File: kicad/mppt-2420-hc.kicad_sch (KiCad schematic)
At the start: 18 parts, among them J1 MKDS 5/ 2-9,5, J2 MKDS 5/ 2-9,5, J3 MKDS 5/ 2-9,5, J4 8P8C, J5 8P8C, J6 JST PH

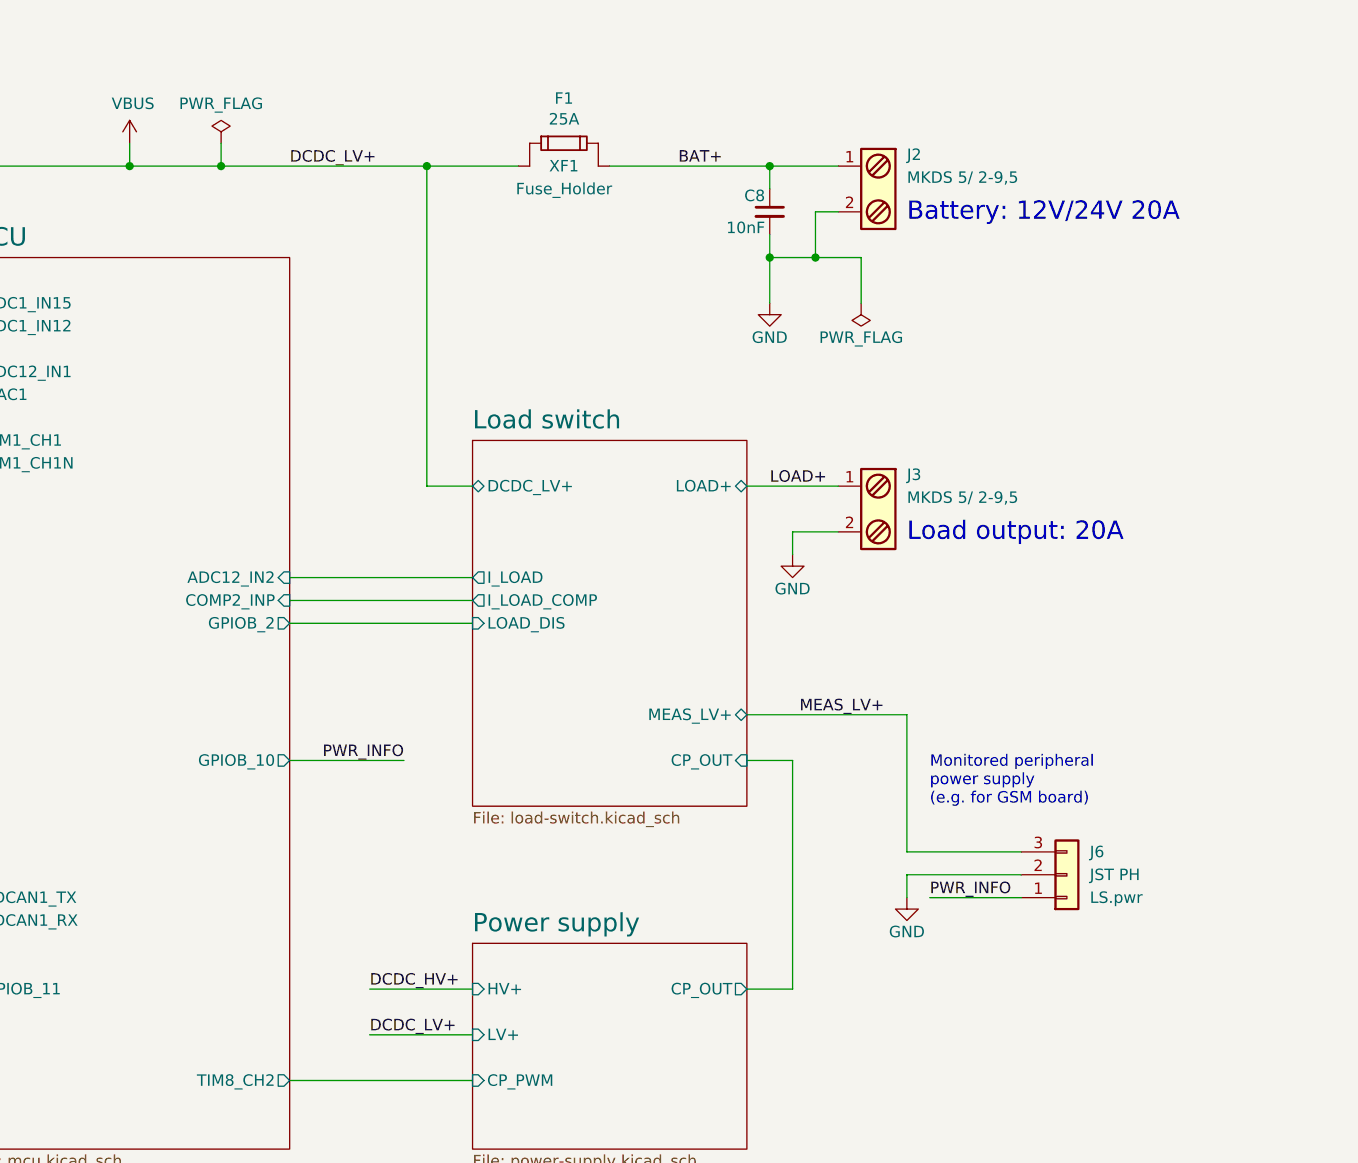
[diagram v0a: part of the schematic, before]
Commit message: removed load terminal & circuit
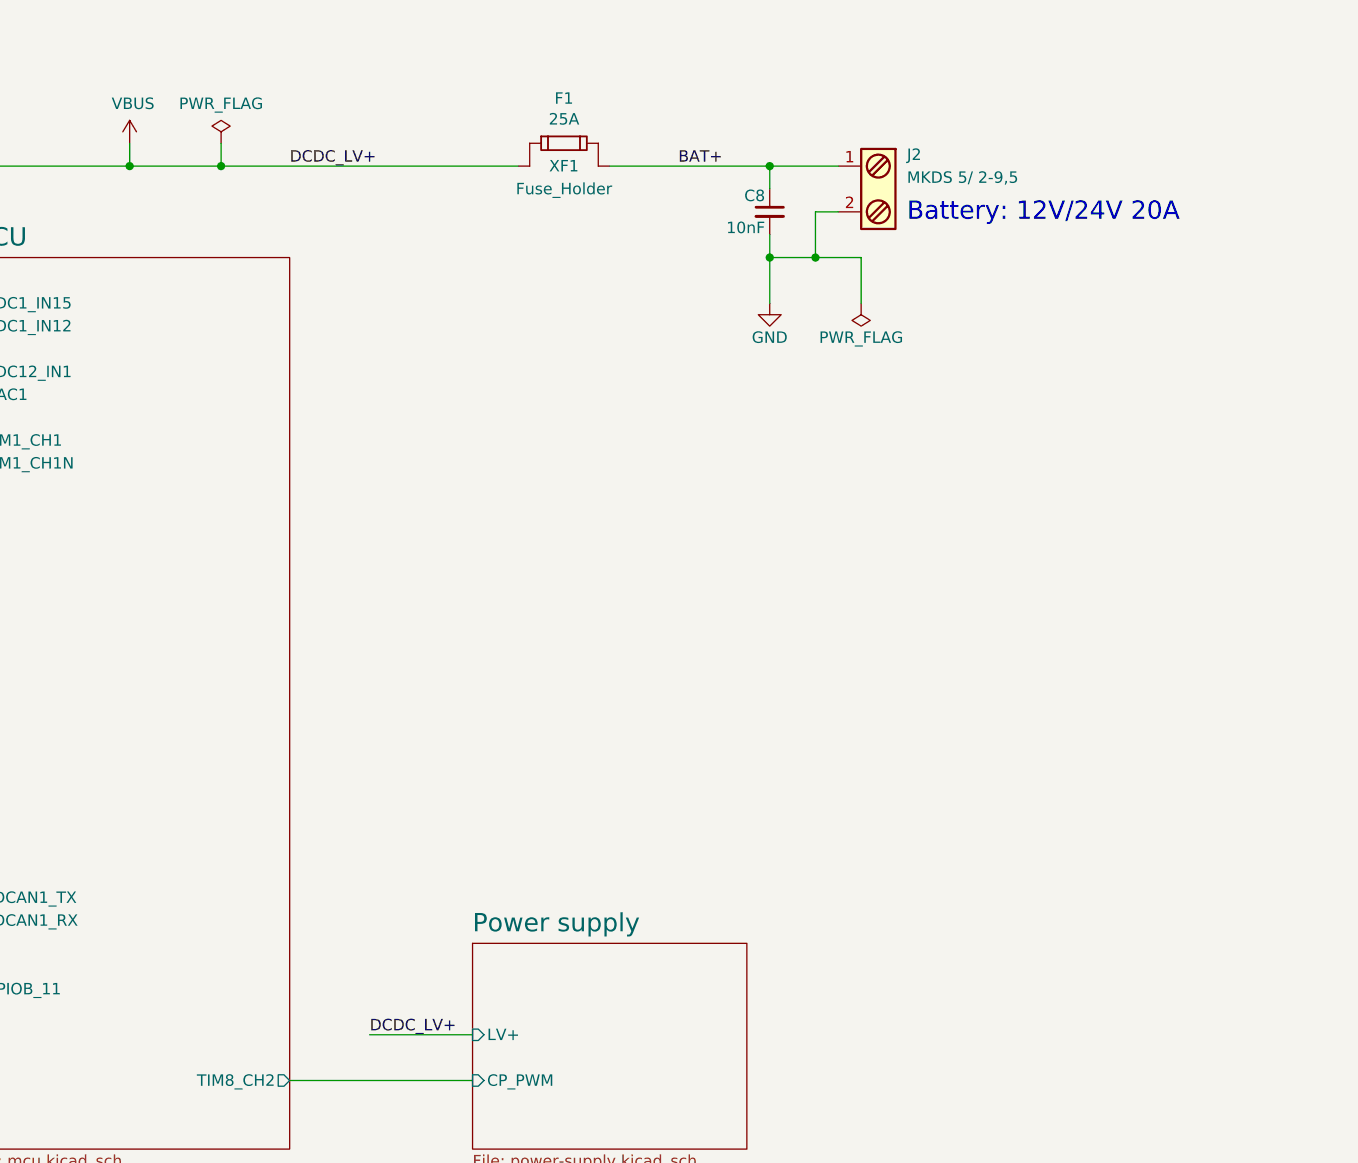
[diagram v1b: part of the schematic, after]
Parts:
- removed J3: MKDS 5/ 2-9,5, LibreSolar:Phoenix_Contact_MKDS_5-2-9,5, symbol Project:Screw_Terminal_1x02
- removed J6: JST PH, Connector_JST:JST_PH_B3B-PH-K_1x03_P2.00mm_Vertical, symbol Connector_Generic:Conn_01x03
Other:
- removed sheet Load switch
- sheet MCU ports: added none; removed ADC12_IN2, COMP2_INP, GPIOB_10, GPIOB_2
- sheet Power supply ports: added none; removed CP_OUT, HV+
- note removed: "Load output: 20A"
- note removed: "Monitored peripheral power supply (e.g. for GSM board)"

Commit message: major changes
removed Load terminal

changed to 6.3x32mm fuse pcb holder

added LibreSolar kicad footprint library locally
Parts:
- XF1: footprint LibreSolar:Keystone-Fuse-3557-2 -> LibreSolar:Eaton_S-400; Manufacturer Keystone -> Eaton; PartNumber 3557-2 -> (none)
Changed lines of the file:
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@@
     (property "Reference" "XF1" (id 0) (at 198.12 48.26 0))
     (property "Value" "Fuse_Holder" (id 1) (at 198.12 50.8 0))
-    (property "Footprint" "LibreSolar:Keystone-Fuse-3557-2" (id 2) (at 198.12 48.26 0)
+    (property "Footprint" "LibreSolar:Eaton_S-400" (id 2) (at 198.12 48.26 0)
       (effects (font (size 1.27 1.27)) hide)
     )
@@
       (effects (font (size 1.27 1.27)) hide)
     )
-    (property "Manufacturer" "Keystone" (id 4) (at 198.12 48.26 0)
-      (effects (font (size 1.27 1.27)) hide)
-    )
-    (property "PartNumber" "3557-2" (id 5) (at 198.12 48.26 0)
+    (property "Manufacturer" "Eaton" (id 4) (at 198.12 48.26 0)
+      (effects (font (size 1.27 1.27)) hide)
+    )
+    (property "PartNumber" "" (id 5) (at 198.12 48.26 0)
       (effects (font (size 1.27 1.27)) hide)
     )
@@
     )
     (path "/00000000-0000-0000-0000-00005eea3888"
-      (reference "XF1") (unit 1) (value "Fuse_Holder") (footprint "LibreSolar:Keystone-Fuse-3557-2")
+      (reference "XF1") (unit 1) (value "Fuse_Holder") (footprint "LibreSolar:Eaton_S-400")
     )
     (path "/00000000-0000-0000-0000-000058a68dcb/00000000-0000-0000-0000-00005daa9f9f"

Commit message: minor component name fix
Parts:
- XF1: footprint LibreSolar:Eaton_S-400 -> LibreSolar:Eaton_S-4000
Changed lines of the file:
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@@
     (property "Reference" "XF1" (id 0) (at 198.12 48.26 0))
     (property "Value" "Fuse_Holder" (id 1) (at 198.12 50.8 0))
-    (property "Footprint" "LibreSolar:Eaton_S-400" (id 2) (at 198.12 48.26 0)
+    (property "Footprint" "LibreSolar:Eaton_S-4000" (id 2) (at 198.12 48.26 0)
       (effects (font (size 1.27 1.27)) hide)
     )
@@
     )
     (path "/00000000-0000-0000-0000-00005eea3888"
-      (reference "XF1") (unit 1) (value "Fuse_Holder") (footprint "LibreSolar:Eaton_S-400")
+      (reference "XF1") (unit 1) (value "Fuse_Holder") (footprint "LibreSolar:Eaton_S-4000")
     )
     (path "/00000000-0000-0000-0000-000058a68dcb/00000000-0000-0000-0000-00005daa9f9f"
